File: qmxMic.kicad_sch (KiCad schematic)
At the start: 11 parts, among them J1 PJ-313, J2 2.54mm, J3 1.27mm, J4 2.54mm, J5 7.62mm, SW1 6mm

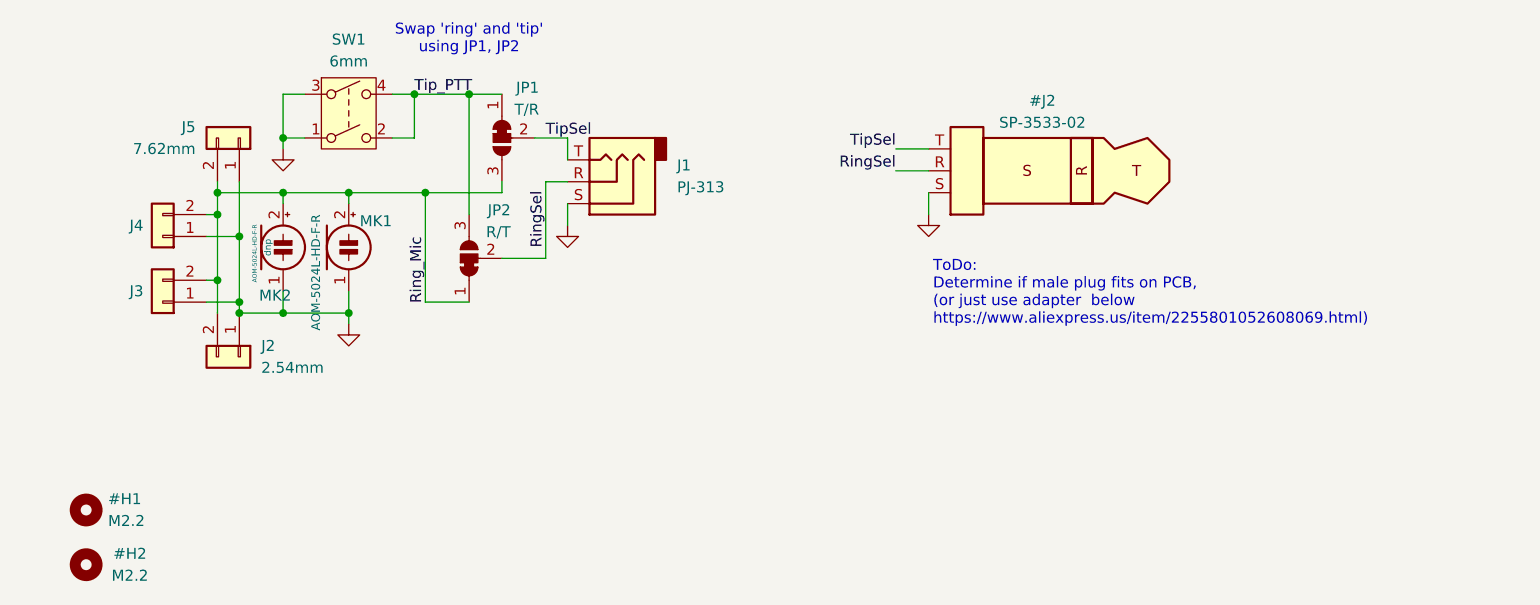
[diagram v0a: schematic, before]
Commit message: Update 'readme.md' to include the qmxMic PCB.  Mark unused connectors as 'dnp'.  Fix copyright year.
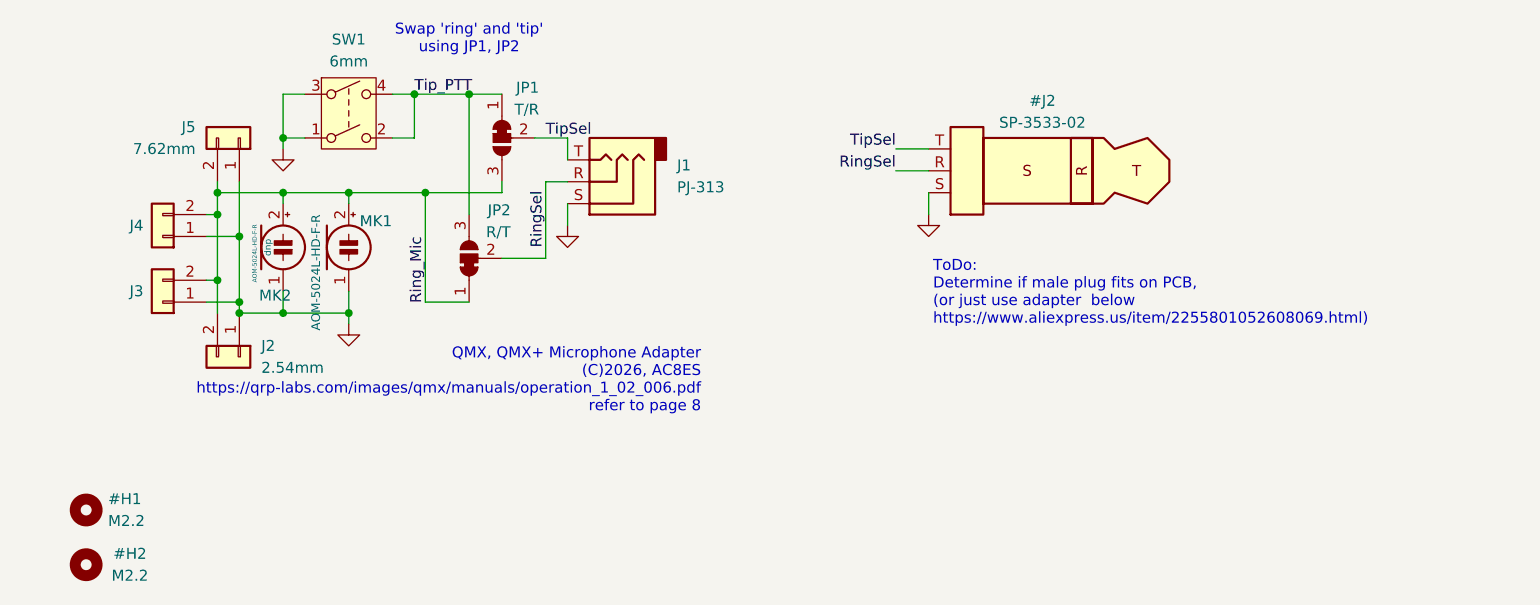
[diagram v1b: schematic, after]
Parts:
- J3, J4, J5: DNP (none) -> dnp
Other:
- note added: "QMX, QMX+ Microphone Adapter (C)2026, AC8ES https://qrp-labs.com/images/qmx/manuals/operation_1_02_006.pdf refer to page 8"

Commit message: Added notes for very low-cost microphone from AliExpress.
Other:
- note added: "ToDo: - Determine if male plug fits on PCB, (or just use adapter below https://www.aliexpress.us/item/2255801052608069.html) - Test this microphone https://www.aliexpress.us/item/3256805663549426.html"
- note removed: "ToDo: Determine if male plug fits on PCB, (or just use adapter below https://www.aliexpress.us/item/2255801052608069.html)"
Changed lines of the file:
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@@
 		)
 	)
-	(text "ToDo:\nDetermine if male plug fits on PCB, \n(or just use adapter  below\nhttps://www.aliexpress.us/item/2255801052608069.html)"
+	(text "ToDo:\n- Determine if male plug fits on PCB, \n(or just use adapter  below\nhttps://www.aliexpress.us/item/2255801052608069.html)\n- Test this microphone\n  https://www.aliexpress.us/item/3256805663549426.html"
 		(exclude_from_sim no)
 		(at 188.468 65.024 0)
@@
 	)
 	(image
-		(at 199.39 72.39)
+		(at 198.12 74.93)
 		(scale 0.5)
 		(data "iVBORw0KGgoAAAANSUhEUgAAAHwAAAAeCAIAAABhQO24AAAACXBIWXMAAAsTAAALEwEAmpwYAAAb"
